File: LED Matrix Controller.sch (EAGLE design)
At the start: 5 parts, among them CN1 LED OUT, CN2 5V PWR, U1 328P

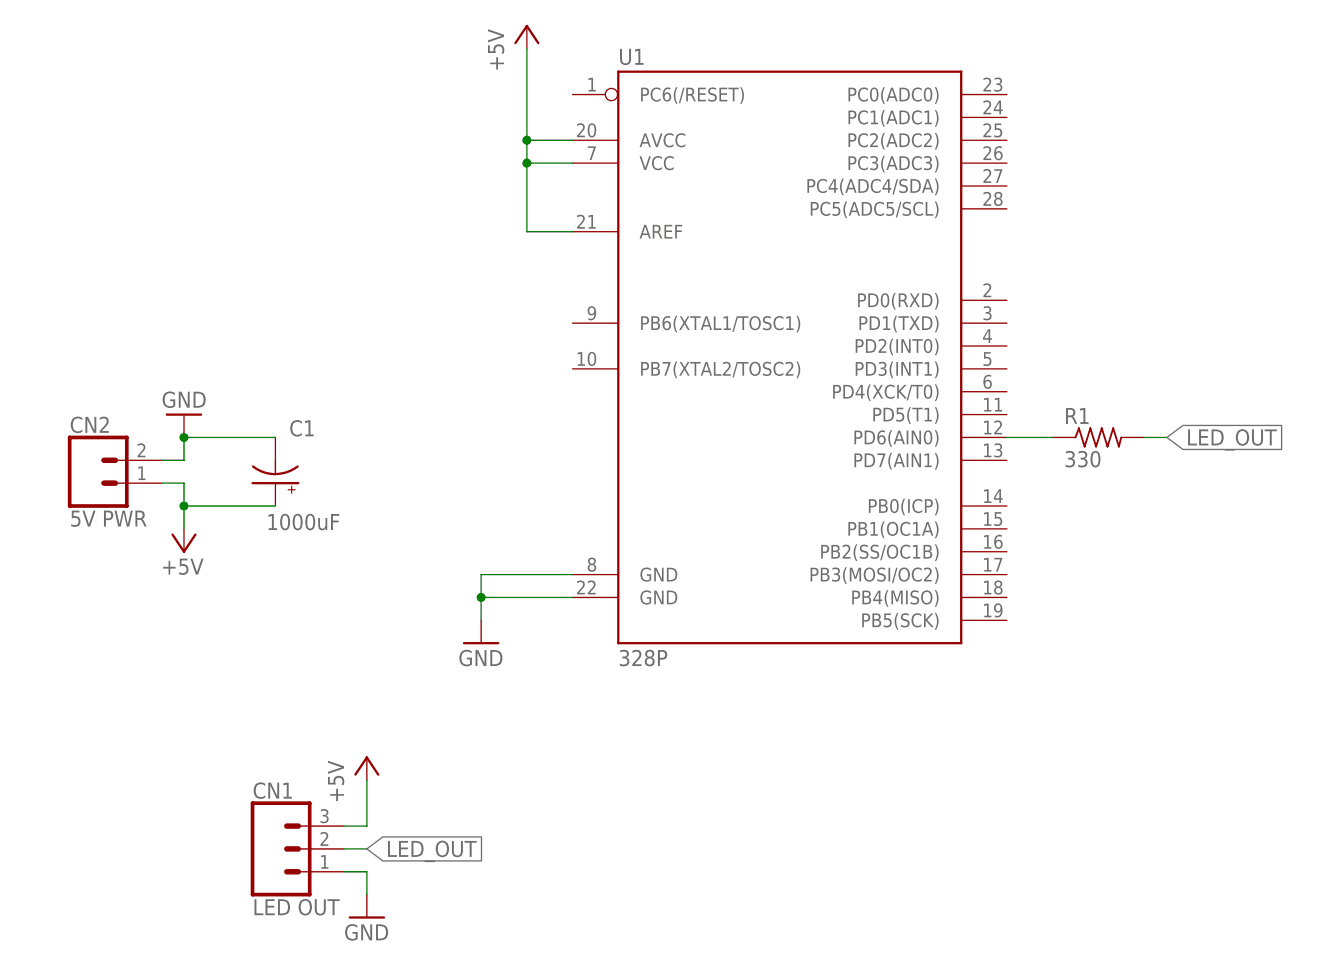
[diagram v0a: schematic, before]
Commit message: Add ISP and serial debug headers
Somewhat useful for not having to remove the chip to reprogram it.
ISP header needs a wire to connect 5v. I thought that wasn't needed
but once I tested it, apparently it is.
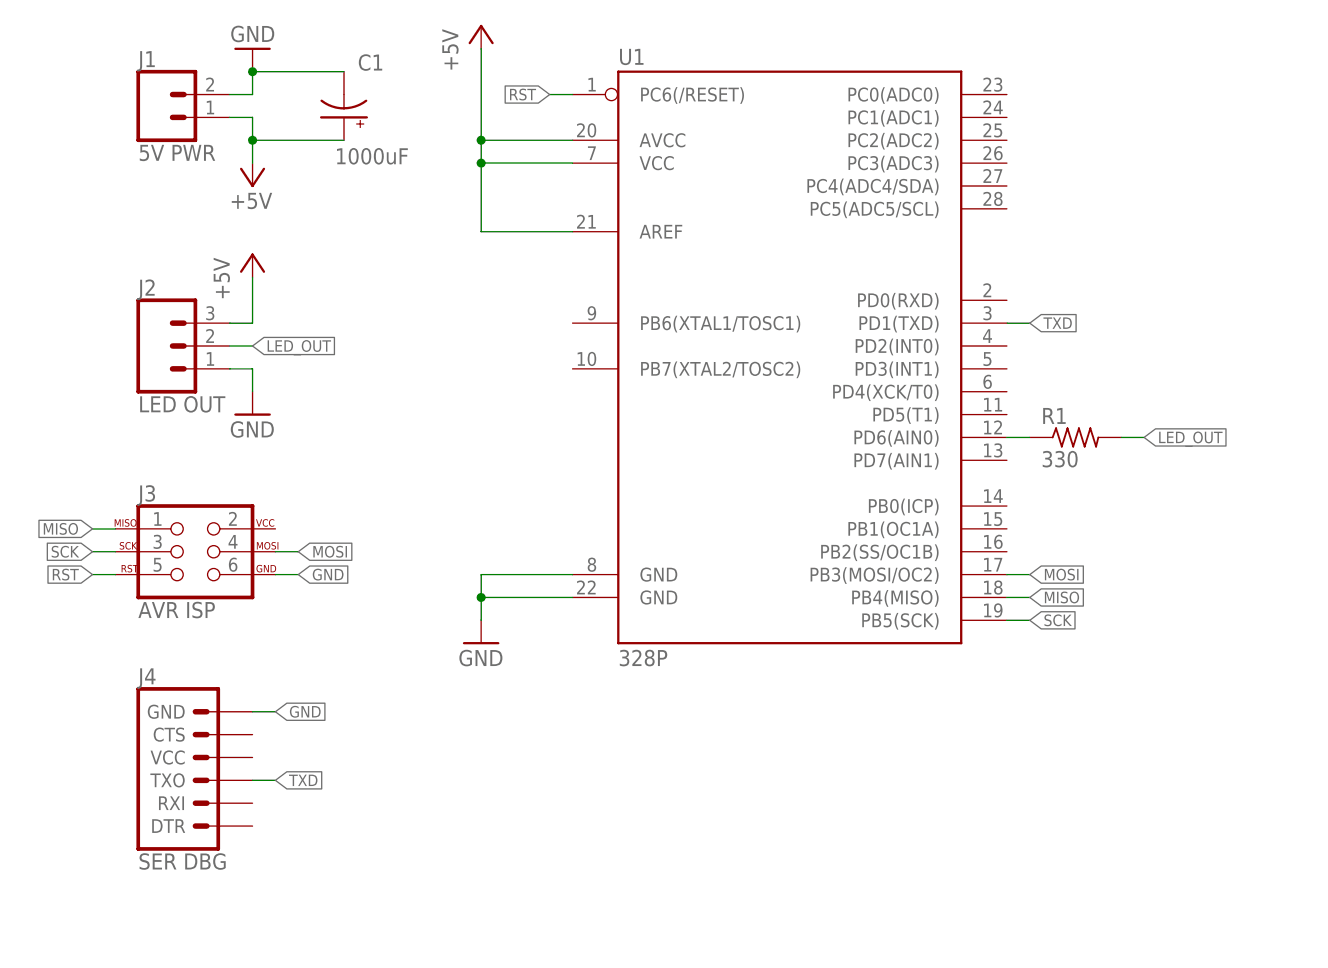
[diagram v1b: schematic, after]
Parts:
- removed CN1: LED OUT, SparkFun-Connectors:CONN_03-SCREW-5MM
- removed CN2: 5V PWR, SparkFun-Connectors:CONN_025MM
- added J1: 5V PWR, SparkFun-Connectors:CONN_025MM
- added J2: LED OUT, SparkFun-Connectors:CONN_03-SCREW-5MM
- added J3: AVR ISP, SparkFun-Connectors:AVR_SPI_PROG_3X2PTH
- added J4: SER DBG, SparkFun-Connectors:6_PIN_SERIAL_TARGETSILK
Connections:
- new net MISO: J3.1, U1.PB4(MISO)
- new net MOSI: J3.4, U1.PB3(MOSI/OC2)
- new net RST: J3.5, U1.PC6(/RESET)
- new net SCK: J3.3, U1.PB5(SCK)
- new net TXD: J4.TXO, U1.PD1(TXD)
- net +5V: now also J1.1, J2.3; no longer CN1.3, CN2.1
- net GND: now also J1.2, J2.1, J3.6, J4.GND; no longer CN1.1, CN2.2
- net LED_OUT: now also J2.2; no longer CN1.2
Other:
- moved on the sheet: C1, R1

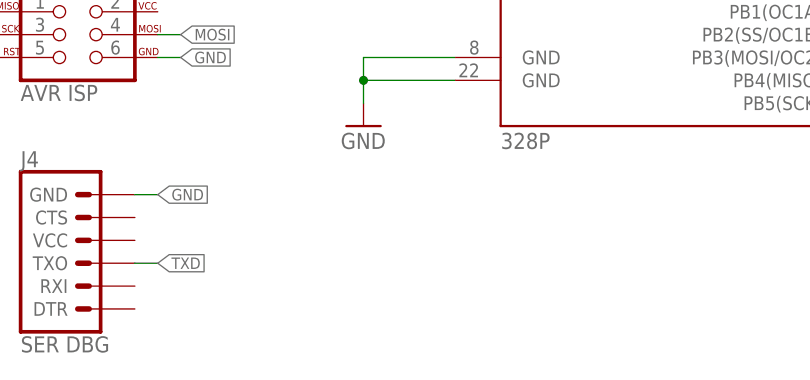
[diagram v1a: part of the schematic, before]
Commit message: Add a reset button
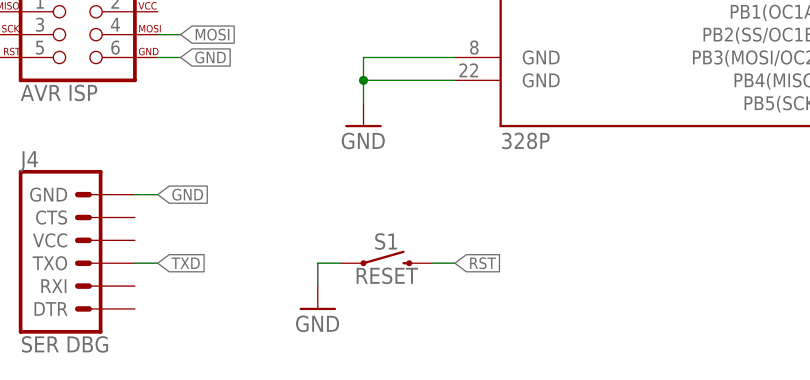
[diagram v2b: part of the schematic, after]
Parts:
- added S1: RESET, SparkFun-Switches:MOMENTARY-SWITCH-SPST-PTH-6.0MM
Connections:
- net GND: now also S1.1
- net RST: now also S1.2
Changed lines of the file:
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@@
 <part name="J3" library="SparkFun-Connectors" library_urn="urn:adsk.eagle:library:513" deviceset="AVR_SPI_PROG_3X2" device="PTH" package3d_urn="urn:adsk.eagle:package:38016/1" value="AVR ISP"/>
 <part name="J4" library="SparkFun-Connectors" library_urn="urn:adsk.eagle:library:513" deviceset="6_PIN_SERIAL_TARGET" device="SILK" package3d_urn="urn:adsk.eagle:package:37995/1" value="SER DBG"/>
+<part name="S1" library="SparkFun-Switches" library_urn="urn:adsk.eagle:library:535" deviceset="MOMENTARY-SWITCH-SPST" device="-PTH-6.0MM" package3d_urn="urn:adsk.eagle:package:40163/1" value="RESET"/>
+<part name="GND1" library="supply1" library_urn="urn:adsk.eagle:library:371" deviceset="GND" device=""/>
 </parts>
 <sheets>
@@
 <attribute name="VALUE" x="30.48" y="76.454" size="1.778" layer="96" font="vector"/>
 <attribute name="NAME" x="30.48" y="97.028" size="1.778" layer="95" font="vector"/>
+</instance>
+<instance part="S1" gate="G$1" x="71.12" y="86.36" smashed="yes">
+<attribute name="NAME" x="71.12" y="87.884" size="1.778" layer="95" font="vector" align="bottom-center"/>
+<attribute name="VALUE" x="71.12" y="85.852" size="1.778" layer="96" font="vector" align="top-center"/>
+</instance>
+<instance part="GND1" gate="1" x="63.5" y="81.28" smashed="yes">
+<attribute name="VALUE" x="60.96" y="78.74" size="1.778" layer="96"/>
 </instance>
 </instances>
@@
 <label x="45.72" y="93.98" size="1.27" layer="95" xref="yes"/>
 </segment>
+<segment>
+<pinref part="S1" gate="G$1" pin="1"/>
+<wire x1="66.04" y1="86.36" x2="63.5" y2="86.36" width="0.1524" layer="91"/>
+<pinref part="GND1" gate="1" pin="GND"/>
+<wire x1="63.5" y1="86.36" x2="63.5" y2="83.82" width="0.1524" layer="91"/>
+</segment>
 </net>
 <net name="N$1" class="0">
@@
 <label x="25.4" y="109.22" size="1.27" layer="95" rot="MR0" xref="yes"/>
 </segment>
+<segment>
+<pinref part="S1" gate="G$1" pin="2"/>
+<wire x1="76.2" y1="86.36" x2="78.74" y2="86.36" width="0.1524" layer="91"/>
+<label x="78.74" y="86.36" size="1.27" layer="95" xref="yes"/>
+</segment>
 </net>

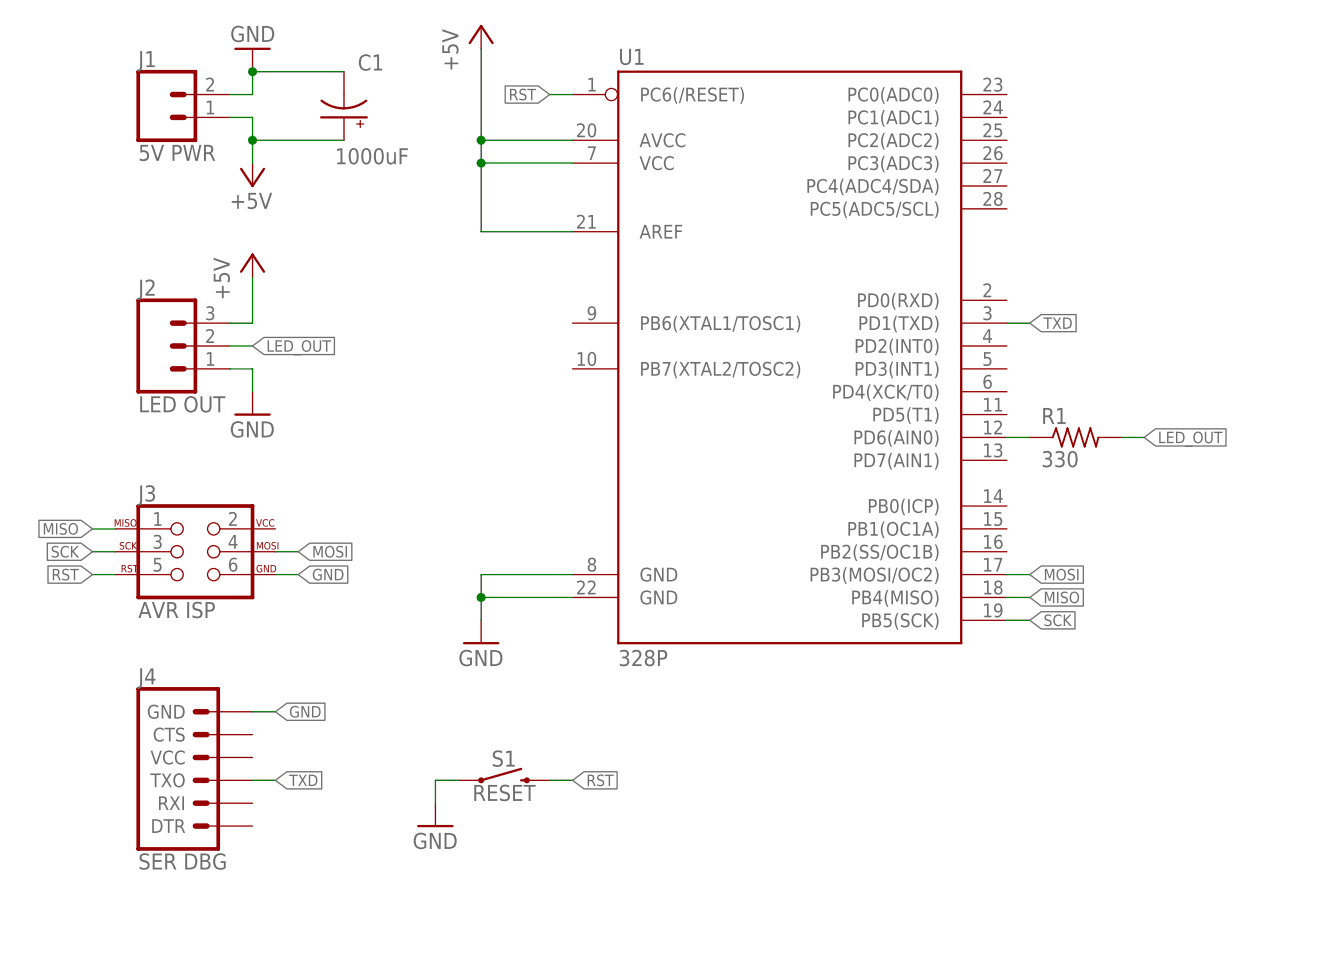
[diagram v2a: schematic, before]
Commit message: Create a two-layer version
A couple of small updates for manufacturing a 2 layer board.  Route
power to the ICSP header and the rest of the FTDI serial header
signals since it's easy now.
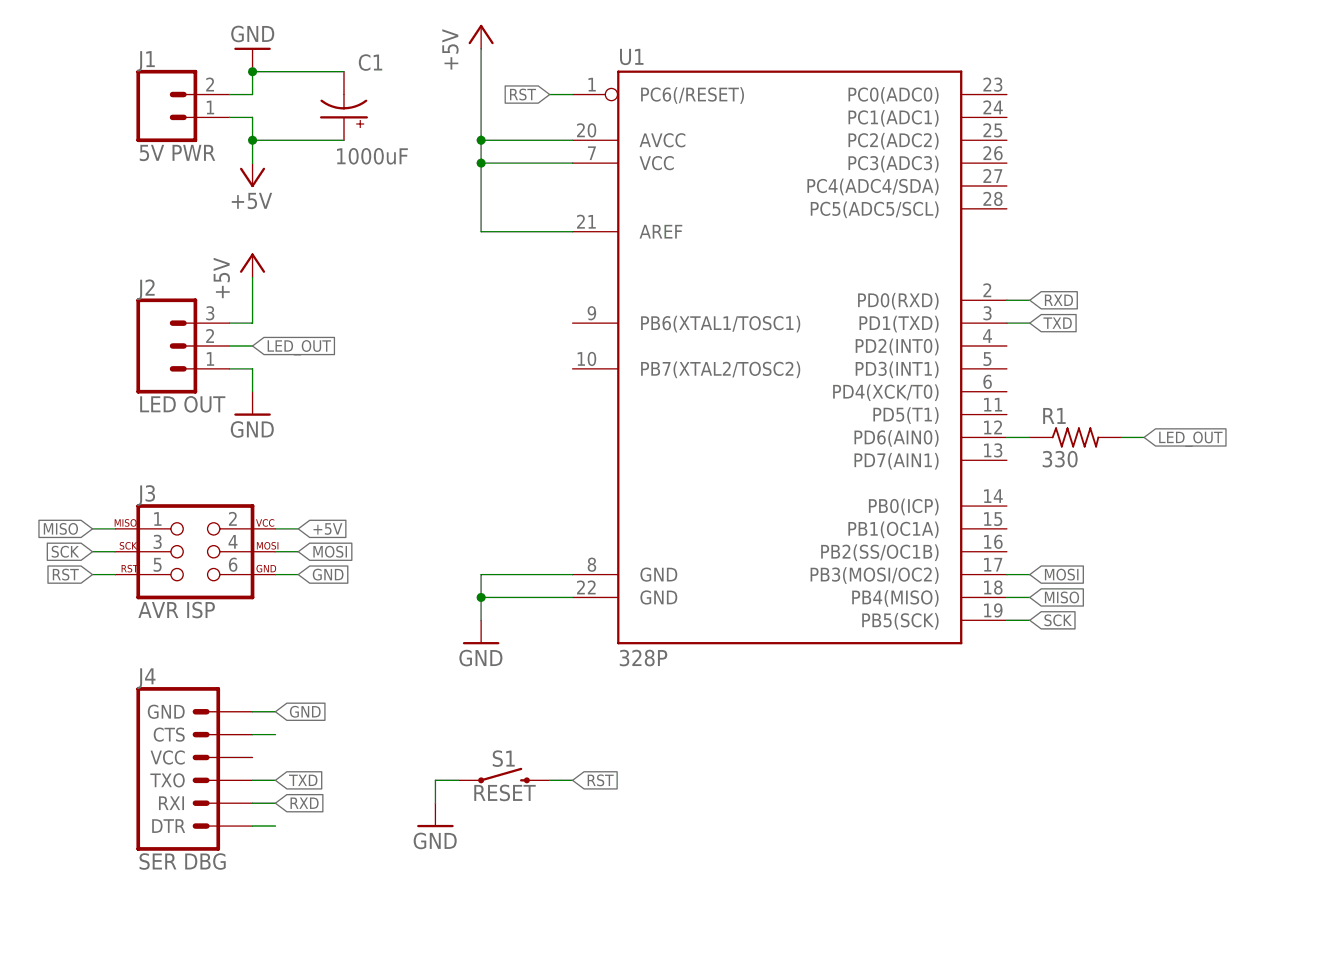
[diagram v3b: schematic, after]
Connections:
- new net N$3: J4.DTR
- new net N$5: J4.CTS
- new net RXD: J4.RXI, U1.PD0(RXD)
- net +5V: now also J3.2
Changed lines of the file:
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@@
 <junction x="43.18" y="157.48"/>
+</segment>
+<segment>
+<pinref part="J3" gate="G$1" pin="2"/>
+<wire x1="45.72" y1="114.3" x2="48.26" y2="114.3" width="0.1524" layer="91"/>
+<label x="48.26" y="114.3" size="1.27" layer="95" xref="yes"/>
 </segment>
 </net>
@@
 </segment>
 </net>
+<net name="N$3" class="0">
+<segment>
+<pinref part="J4" gate="G$1" pin="DTR"/>
+<wire x1="43.18" y1="81.28" x2="45.72" y2="81.28" width="0.1524" layer="91"/>
+</segment>
+</net>
+<net name="N$5" class="0">
+<segment>
+<pinref part="J4" gate="G$1" pin="CTS"/>
+<wire x1="43.18" y1="91.44" x2="45.72" y2="91.44" width="0.1524" layer="91"/>
+</segment>
+</net>
+<net name="RXD" class="0">
+<segment>
+<pinref part="U1" gate="G$1" pin="PD0(RXD)"/>
+<wire x1="127" y1="139.7" x2="129.54" y2="139.7" width="0.1524" layer="91"/>
+<label x="129.54" y="139.7" size="1.27" layer="95" xref="yes"/>
+</segment>
+<segment>
+<pinref part="J4" gate="G$1" pin="RXI"/>
+<wire x1="43.18" y1="83.82" x2="45.72" y2="83.82" width="0.1524" layer="91"/>
+<label x="45.72" y="83.82" size="1.27" layer="95" xref="yes"/>
+</segment>
+</net>
